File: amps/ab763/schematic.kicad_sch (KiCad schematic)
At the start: 116 parts, among them T1 125P33A, T2 125C3A, T3 125A1A, T4 125A20B

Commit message: Fix: the AB763 phase inverter's two halves sat on the wrong pins, on both the sheet and the board
On the C-FD layout page the 12AT7 inverter's +170 V plate lead, the 82k (hot)
side that the mix node's .001 feeds, lands on pin 1. The +180 V plate (the
100k, cold side) lands on pin 6, and +77 V is on the joined cathodes. The hot
half is therefore unit 2 (pins 1/2/3) and the cold half unit 1 (6/7/8). The
sheet drew V6A/V6B at the default map (A → unit 1), and the board wired the
hot plate, grid and coupler to pins 6/7 and the cold ones to 1/2. The two
surfaces agreed with each other and both disagreed with the page, so the
sheet↔board check could not see it. The blackface board agent found it; it
is confirmed here at native size (layout 6026 × 3650).

- Sheet: V6A unit=2, V6B unit=1, citing the page.
- Board: pins 1↔6, 2↔7, 3↔8 exchanged on the eight inverter runs (both plate
  loads, both couplers C1/C2, both grid leaks, both cathodes to the tail).
  Vias fanned with pipeline/_route.py.

verify_schematic_nets ab763: PASS (claimed). verify_layout_nets ab763: PASS
(the checker solves the section assignment, so no modelled net moves).
Collision lint 0. Both claims keep their fields. What changes is the pin
numbering both drawings print, which is a fact under each claim.

Co-Authored-By: Claude Opus 5 (1M context) <noreply@anthropic.com>
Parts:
- V6A: Basing_unit (none) -> 2
- V6B: Basing_unit (none) -> 1
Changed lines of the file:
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@@
     (in_bom yes) (on_board yes)
     (property "Reference" "V6A" (at 273.7 69.878 0) (effects (font (size 1.27 1.27)) (justify left)))
-    (property "Value" "12AT7" (at 273.7 72.278 0) (effects (font (size 1.27 1.27)) (justify left))))
+    (property "Value" "12AT7" (at 273.7 72.278 0) (effects (font (size 1.27 1.27)) (justify left)))
+    (property "Basing_unit" "2" (at 273.7 74.678 0) (effects (font (size 1.27 1.27)) hide)))
   (symbol (lib_id "cx:TRIODE") (at 267.7 108.278 0) (unit 1)
     (in_bom yes) (on_board yes)
     (property "Reference" "V6B" (at 273.7 101.878 0) (effects (font (size 1.27 1.27)) (justify left)))
-    (property "Value" "12AT7" (at 273.7 104.278 0) (effects (font (size 1.27 1.27)) (justify left))))
+    (property "Value" "12AT7" (at 273.7 104.278 0) (effects (font (size 1.27 1.27)) (justify left)))
+    (property "Basing_unit" "1" (at 273.7 106.678 0) (effects (font (size 1.27 1.27)) hide)))
   (wire (pts (xy 267.7 68.658) (xy 267.7 65.178))
     (stroke (width 0) (type default)))
@@
   (text "3" (at 106.55 192.628 0)
     (effects (font (size 1.1 1.1)) (justify left)))
-  (text "6" (at 268.55 69.928 0)
-    (effects (font (size 1.1 1.1)) (justify left)))
-  (text "7" (at 260.753 74.878 0)
-    (effects (font (size 1.1 1.1)) (justify left)))
-  (text "8" (at 270 82.628 0)
-    (effects (font (size 1.1 1.1)) (justify left)))
-  (text "1" (at 268.55 101.928 0)
-    (effects (font (size 1.1 1.1)) (justify left)))
-  (text "2" (at 260.753 106.878 0)
-    (effects (font (size 1.1 1.1)) (justify left)))
-  (text "3" (at 268.55 114.628 0)
+  (text "1" (at 268.55 69.928 0)
+    (effects (font (size 1.1 1.1)) (justify left)))
+  (text "2" (at 260.753 74.878 0)
+    (effects (font (size 1.1 1.1)) (justify left)))
+  (text "3" (at 270 82.628 0)
+    (effects (font (size 1.1 1.1)) (justify left)))
+  (text "6" (at 268.55 101.928 0)
+    (effects (font (size 1.1 1.1)) (justify left)))
+  (text "7" (at 260.753 106.878 0)
+    (effects (font (size 1.1 1.1)) (justify left)))
+  (text "8" (at 268.55 114.628 0)
     (effects (font (size 1.1 1.1)) (justify left)))
   (text "3" (at 330.55 61.293 0)

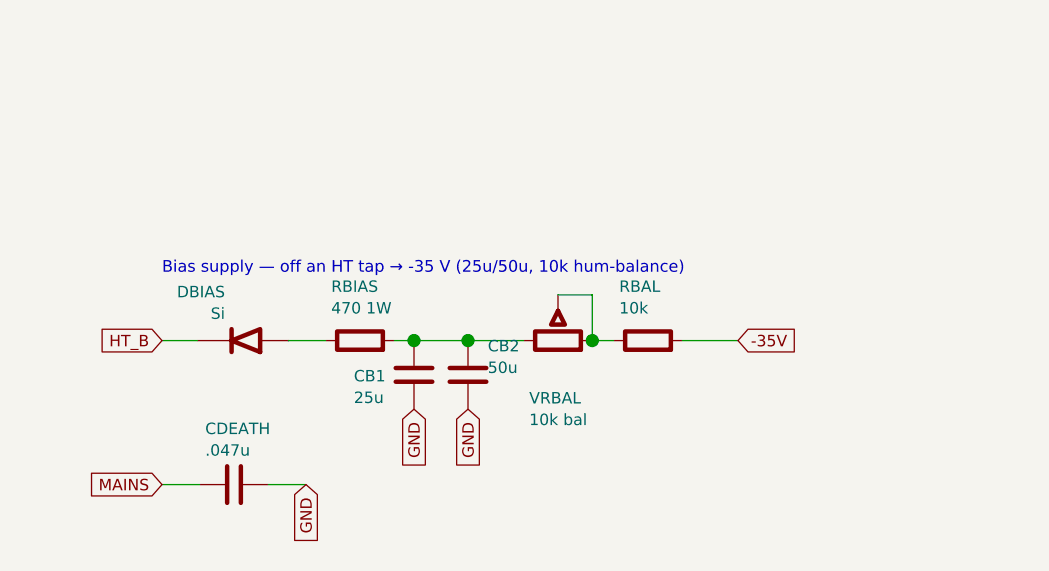
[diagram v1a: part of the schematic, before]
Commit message: Fix: the AB763 sheet drew the bias control as a rheostat in series; the drawing divides the raw supply to ground
The C-FD schematic, read at native size, runs the 10K-L bias control from the
raw negative supply (the node with the rectifier, the 470 and the 25/50 µF
cans) to a 10k (RBAL) that returns to ground. The −35 V line to the 6V6 grid
leaks is the control's WIPER. The sheet drew the control as a rheostat in
series with RBAL and took −35 V off RBAL's far end, so there was no path to
ground at all. The board's own declaration had already read it right: "the
schematic hangs it from the pot's end to ground".

- Sheet: VRBAL across raw → RBAL → ground, with −35 V off the wiper. The raw
  end is labelled BIAS RAW, where the tremolo's 2.2M returns (next commit).
- bom.yaml: VRBAL and RBAL roles say what each joins.
The netlist drives the bias line as an ideal −35 V source, so no DC point
moves. The sheet's bias row is not DC-checked.

Co-Authored-By: Claude Opus 5 (1M context) <noreply@anthropic.com>
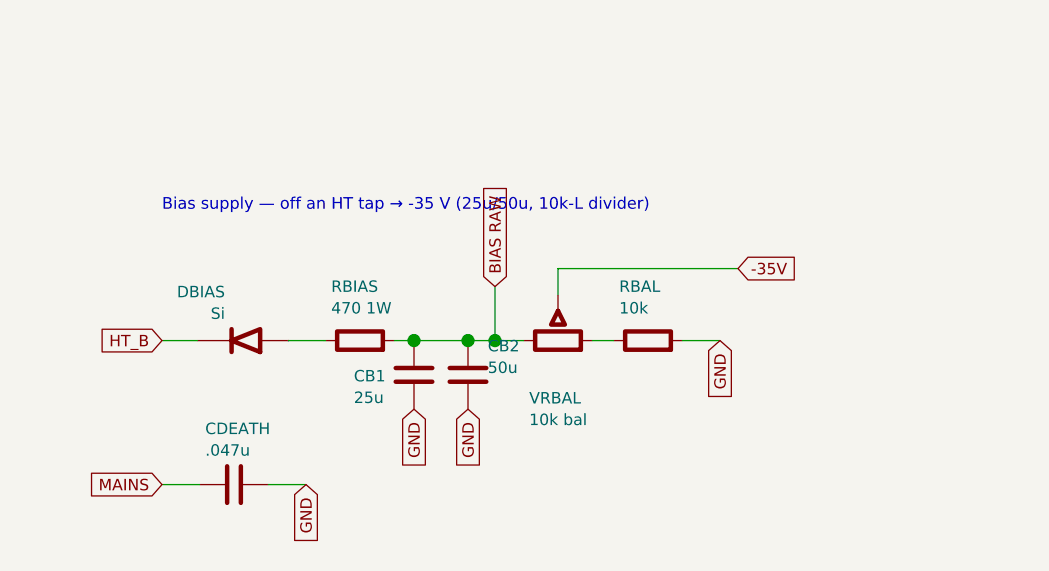
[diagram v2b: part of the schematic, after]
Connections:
- net -35V: now also VRBAL.2 (W); no longer RBAL.2
- net GND: now also RBAL.2
- net BIAS RAW: now reaches CB1.1, CB2.1, RBIAS.2, VRBAL.1
- net at RBAL.1, VRBAL.3: no longer VRBAL.2 (W)
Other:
- note added: "Bias supply — off an HT tap → -35 V (25u/50u, 10k-L divider)"
- note removed: "Bias supply — off an HT tap → -35 V (25u/50u, 10k hum-balance)"
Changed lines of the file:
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@@
   (global_label "GND" (shape input) (at 173.7 241.898 270)
     (effects (font (size 1.27 1.27)) (justify right)))
-  (text "Bias supply — off an HT tap → -35 V (25u/50u, 10k hum-balance)" (at 199.7 212.278 0)
+  (text "Bias supply — off an HT tap → -35 V (25u/50u, 10k-L divider)" (at 199.7 205.278 0)
     (effects (font (size 1.3 1.3)) (justify left)))
   (global_label "HT_B" (shape input) (at 199.7 220.278 180)
@@
   (global_label "GND" (shape input) (at 233.7 227.898 270)
     (effects (font (size 1.27 1.27)) (justify right)))
-  (wire (pts (xy 233.7 220.278) (xy 239.7 220.278))
+  (wire (pts (xy 233.7 220.278) (xy 236.7 220.278))
+    (stroke (width 0) (type default)))
+  (wire (pts (xy 236.7 220.278) (xy 239.89 220.278))
     (stroke (width 0) (type default)))
   (symbol (lib_id "cx:POT") (at 243.7 220.278 90) (unit 1)
@@
     (property "Reference" "VRBAL" (at 240.5 226.678 270) (effects (font (size 1.27 1.27)) (justify left)))
     (property "Value" "10k bal" (at 240.5 229.078 270) (effects (font (size 1.27 1.27)) (justify left))))
-  (wire (pts (xy 239.7 220.278) (xy 239.89 220.278))
+  (wire (pts (xy 243.7 215.198) (xy 243.7 212.278))
     (stroke (width 0) (type default)))
-  (wire (pts (xy 243.7 215.198) (xy 247.51 215.198))
+  (wire (pts (xy 243.7 212.278) (xy 263.7 212.278))
     (stroke (width 0) (type default)))
-  (wire (pts (xy 247.51 215.198) (xy 247.51 220.278))
-    (stroke (width 0) (type default)))
-  (junction (at 247.51 220.278) (diameter 1.467) (color 0 0 0 0))
+  (global_label "-35V" (shape input) (at 263.7 212.278 0)
+    (effects (font (size 1.27 1.27)) (justify left)))
   (symbol (lib_id "cx:R") (at 253.7 220.278 90) (unit 1)
     (in_bom yes) (on_board yes)
@@
   (wire (pts (xy 247.51 220.278) (xy 249.89 220.278))
     (stroke (width 0) (type default)))
-  (wire (pts (xy 257.51 220.278) (xy 263.7 220.278))
+  (wire (pts (xy 257.51 220.278) (xy 261.7 220.278))
     (stroke (width 0) (type default)))
-  (global_label "-35V" (shape input) (at 263.7 220.278 0)
+  (global_label "GND" (shape input) (at 261.7 220.278 270)
+    (effects (font (size 1.27 1.27)) (justify right)))
+  (junction (at 236.7 220.278) (diameter 1.467) (color 0 0 0 0))
+  (wire (pts (xy 236.7 220.278) (xy 236.7 214.278))
+    (stroke (width 0) (type default)))
+  (global_label "BIAS RAW" (shape input) (at 236.7 214.278 90)
     (effects (font (size 1.27 1.27)) (justify left)))
   (global_label "MAINS" (shape input) (at 199.7 236.278 180)

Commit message: Fix: the AB763 tremolo was drawn as a circuit the drawing does not have
The C-FD schematic, read at native size, draws the tremolo as follows:
- V5A is a phase-shift oscillator. Its plate feeds a .02 → .01 → .01 ladder
  back to its own grid. The ladder's middle node goes to ground through the
  3M-RA Speed rheostat and a 100k. The outer node and the grid each reach the
  vibrato-pedal node through a 1M. A 2.2M returns that node to the raw
  negative bias supply, the node ahead of the 10K-L bias control, and the
  footswitch grounds it.
- V5B's grid is DC-coupled to the ladder's outer node. Its plate (+345 V) is
  fed from +415 V (box [B]) through a 10M, and through the neon lamp and a
  100k in series. Both cathodes are bypassed: 2.7k and 100k, each with
  25 µF.
- The photocell sits in the 50K-RA Intensity control's wiper. Intensity's
  top takes the node between the mix driver's .1 and its 220k (the mix
  output, sheet label TREM), and its bottom goes to ground.
The sheet had instead drawn a different oscillator:
- plate loads to B+4;
- the .02 into V5B's grid, with the 10M as V5B's grid leak and the 2.2M as
  V5A's grid leak;
- a plate-to-grid ladder with 1Ms to ground;
- Intensity in the lamp's drive;
- the photocell on the mix-driver grid.
It also lacked both cathode bypass caps and the lamp's 100k. The tremolo is
excluded from the DC netlist (V5 declared in meta.yaml `sections:`), so no
gate compared it with anything. The blackface board agent's independent read
agrees on the 2.2M's return.

- Sheet: the tremolo block redrawn as above. The 2.2M takes the BIAS RAW
  label from the previous commit, and a TREM label marks the mix output.
  MIXG no longer carries the photocell. check_schematics: no isolated pins.
  A per-anchor scan finds no dangling label.
- bom.yaml: CKTO1 and CKTO2 (25 µF · 25 V) and RLAMP (100 kΩ) added. Every
  tremolo part's role now says what it joins. RTO1 is the speed network's
  100k to ground, as the layout also letters it, not a plate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
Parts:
- removed C13: 16u, symbol cx:C
- removed RBIAS: 470 1W, symbol cx:R
- removed RLPA: 82k 5%, symbol cx:R
- removed RNFB: 820, symbol cx:R
- removed RTOG3: 1M, symbol cx:R
- removed T1: 125P33A, symbol cx:PT
- added CB2: 50u, symbol cx:C
- added CTO3: .02u, symbol cx:C
- added RBAL: 10k, symbol cx:R
- added RGPB: 1M, symbol cx:R
- added RLAMP: 100k, symbol cx:R
- added RTOG: 2.2M, symbol cx:R
- added V8: 6V6GT, symbol cx:PENTODE
- added V9B: GZ34, symbol cx:DIODE_TUBE
- added VRINT: 50k int, symbol cx:POT
- C13: renamed from CB2; value 50u -> 16u
- C2: renamed from V8; value 6V6GT -> .1u; symbol cx:PENTODE -> cx:C
- CKTO1: renamed from RTOG; value 2.2M -> 25u; symbol cx:R -> cx:C
- CKTO2: renamed from VRINT; value 50k int -> 25u; symbol cx:POT -> cx:C
- RBIAS: renamed from RBAL; value 10k -> 470 1W
- RLPA: renamed from RTAIL; value 470 -> 82k 5%
- RNFB: renamed from C2; value .1u -> 820; symbol cx:C -> cx:R
- RTAIL: renamed from RGPB; value 1M -> 470
- RTOG3: renamed from CTO3; value .02u -> 1M; symbol cx:C -> cx:R
- T1: renamed from V9B; value GZ34 -> 125P33A; symbol cx:DIODE_TUBE -> cx:PT
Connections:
- net B+1: now also V9B.2 (K); no longer T1.2 (K), T4.2 (PRI_B)
- net B+2: now also RTO10.1, RTO2.1, RLAMP.1
- net B+3: now also RLPA.1
- net B+4: now also C13.1; no longer RTO1.1, RTO2.1
- net BIAS RAW: now also RBIAS.2, CB2.1, RTOG.2; no longer C13.1
- net GND: now also CKTO2.2, RTO1.2, T1.4 (HT_CT), CB2.2, RBAL.2, V8.4 (K), VRINT.1; no longer C2.4 (K), CKTO2.3, OPTO.2 (L2), RBIAS.2, RTO10.2, RTOG2.2, VRSPD.3
- net HT_A: now also T1.3 (HT_A)
- net HT_B: now also T1.5 (HT_B), V9B.1 (A); no longer T1.1 (A)
- net MAINS: now also T1.1 (PRI_1)
- net MAINS N: now also T1.2 (PRI_2)
- net MIXG: no longer OPTO.3 (P1)
- net SPKR: now also RNFB.1
- net at RKTO2.1, V5B.3 (K): now also CKTO2.1
- net at CPIB.1, RNF2.1: now also RNFB.2
- net at RLPB.2, V6B.1 (P): now also C2.1; no longer RNFB.1
- net at C2.2, RGL2.1: now also V8.2 (G1); no longer RNFB.2
- net at VRBN.1, VRBN.2 (W), VRTN.3: no longer CBN.2
- net at RTO2.2, V5A.1 (P): now also CTO3.2; no longer CTO1.2, RTOG3.1
- net at RKTO1.1, V5A.3 (K): now also CKTO1.1
- net at V4A.1 (P), V4B.1 (P): no longer T4.1 (PRI_P)
- net at T3.3 (PRI_B): now also V8.1 (P); no longer C2.1 (P)
- net at RS2.1: now also V8.3 (G2); no longer C2.3 (G2)
- net at CPIB.2, V6B.2 (G): now also RGPB.2; no longer RTAIL.2
- net at V6A.3 (K), V6B.3 (K): now also RTAIL.2; no longer RLPA.2
- net at C1.1, V6A.1 (P): now also RLPA.2
- net at RSLN.1, VRBN.3: no longer CBN2.2
- net at CBV.2, VRBV.1, VRTV.3: no longer VRBV.2 (W)
- net at RGPA.2, RT2.1, RTAIL.1: now also RGPB.1; no longer RLPA.1
- net at OPTO.1 (L1): now also RLAMP.2; no longer CKTO2.2 (W)
- net at CBRV.1, VRVV.1: no longer VRTV.2 (W)
- net TREM: now reaches CCD1.2, RMD1.1
- net TREM: now also VRINT.3
- net at DBIAS.1 (A): now also RBIAS.1
- net at VRBAL.3: now also RBAL.1; no longer RBIAS.1
- new net: OPTO.2 (L2), RTO10.2, V5B.1 (P)
- new net: RTO1.1, VRSPD.2 (W), VRSPD.3
- new net: CTO1.2, RTOG3.2, V5A.2 (G)
- new net: OPTO.3 (P1), VRINT.2 (W)
- new net LFO: CTO1.1, CTO2.1, RTOG2.2
- new net SPEED: CTO2.2, CTO3.1, VRSPD.1
- new net VIB PEDAL: RTOG.1, RTOG2.1, RTOG3.1
- now unconnected: V5B.2 (G)
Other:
- note added: "Tremolo (V5) + optocoupler — a running oscillator, excluded from the DC netlist"
- note removed: "Tremolo oscillator (V5) + optocoupler — dynamic; DC point excluded from netlist (see the circuit story)"
- moved on the sheet: C13, CBD1, CBN, CBN2, CBRV, CBV, CBV2, CCD1, CCN2, CCR1, CCV2, CKN1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

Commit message: Fix: letter the AB763 tremolo bottle's sections as the factory layout pins them
On the C-FD layout page the tremolo 12AX7's +270 V oscillator plate is pin 1,
with the +2.1 V cathode on pin 3. The +345 V lamp-driver plate therefore sits
on pin 6. The sheet had drawn both sections at the default map (A → unit 1).
They are now stated: V5A unit=2, V5B unit=1. The board drawn in the next
commit wires them the same way.

Co-Authored-By: Claude Opus 5 (1M context) <noreply@anthropic.com>
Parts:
- V5A: Basing_unit (none) -> 2
- V5B: Basing_unit (none) -> 1
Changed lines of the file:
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@@
     (in_bom yes) (on_board yes)
     (property "Reference" "V5A" (at 73.6088 195.878 0) (effects (font (size 1.27 1.27)) (justify left)))
-    (property "Value" "12AX7" (at 73.6088 198.278 0) (effects (font (size 1.27 1.27)) (justify left))))
+    (property "Value" "12AX7" (at 73.6088 198.278 0) (effects (font (size 1.27 1.27)) (justify left)))
+    (property "Basing_unit" "2" (at 73.6088 200.678 0) (effects (font (size 1.27 1.27)) hide)))
   (wire (pts (xy 43.6088 202.278) (xy 59.9888 202.278))
     (stroke (width 0) (type default)))
@@
     (in_bom yes) (on_board yes)
     (property "Reference" "V5B" (at 113.609 195.878 0) (effects (font (size 1.27 1.27)) (justify left)))
-    (property "Value" "12AX7" (at 113.609 198.278 0) (effects (font (size 1.27 1.27)) (justify left))))
+    (property "Value" "12AX7" (at 113.609 198.278 0) (effects (font (size 1.27 1.27)) (justify left)))
+    (property "Basing_unit" "1" (at 113.609 200.678 0) (effects (font (size 1.27 1.27)) hide)))
   (wire (pts (xy 93.6088 202.278) (xy 99.9888 202.278))
     (stroke (width 0) (type default)))
@@
   (text "8" (at 224.459 156.628 0)
     (effects (font (size 1.1 1.1)) (justify left)))
-  (text "6" (at 68.4588 195.928 0)
-    (effects (font (size 1.1 1.1)) (justify left)))
-  (text "7" (at 60.6616 200.878 0)
-    (effects (font (size 1.1 1.1)) (justify left)))
-  (text "8" (at 68.4588 208.628 0)
-    (effects (font (size 1.1 1.1)) (justify left)))
-  (text "1" (at 108.459 195.928 0)
-    (effects (font (size 1.1 1.1)) (justify left)))
-  (text "2" (at 100.662 200.878 0)
-    (effects (font (size 1.1 1.1)) (justify left)))
-  (text "3" (at 108.459 208.628 0)
+  (text "1" (at 68.4588 195.928 0)
+    (effects (font (size 1.1 1.1)) (justify left)))
+  (text "2" (at 60.6616 200.878 0)
+    (effects (font (size 1.1 1.1)) (justify left)))
+  (text "3" (at 68.4588 208.628 0)
+    (effects (font (size 1.1 1.1)) (justify left)))
+  (text "6" (at 108.459 195.928 0)
+    (effects (font (size 1.1 1.1)) (justify left)))
+  (text "7" (at 100.662 200.878 0)
+    (effects (font (size 1.1 1.1)) (justify left)))
+  (text "8" (at 108.459 208.628 0)
     (effects (font (size 1.1 1.1)) (justify left)))
   (text "1" (at 266.459 69.928 0)

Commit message: Fix: the AB763 sheet grounded the phase inverter's tail; it now ends at the feedback node
The claim fields are untouched. This follows the model change in the previous
commit, from the same C-FD reading (schematic page, crop sch-pi-tail, 740 x 1080
at 2560,680 of the 6070 x 4274 native image): the 22K's far end is a junction
on the vertical lead that brings the 820 down from the speaker, with the
.1-200 from the cold grid and the 47 to ground hanging below it.

- Sheet (pipeline/draw_ab763.py, regenerated): RT2's foot drops onto CPIB's
  far-side wire, the feedback node, in place of its ground symbol, with a
  junction where it lands. RT2.2 now shares a net with RNF2.1, RNFB.2 and
  CPIB.1. verify_schematic_nets ab763: PASS (claimed), with RNFB, now in the
  model, checked end to end. check_schematics: 0 failures, connectivity clean
  (no isolated pin, no dangling label, no shorted part). The preview
  (pipeline/_sch_preview.py) of the inverter was looked at before and after:
  the only change is the foot, and the RT2 / 22k lettering sits where it did.
- bom.yaml: the RT2, RNFB and RNF2 roles say what they join.
- notes.md: the inverter paragraph names the tail's foot and the 47. The chart
  paragraph said the inverter plates and tail "fall within a tenth" of the
  chart; the 82k plate is 10.5 % high, so it now says "about a tenth" and
  names that plate.

reference/sheet-board.yaml is re-exported: RT2 is MISPLACED on ab763 (the
board still grounds the tail) until the board follows in the next commit, so
verify_layout_nets ab763 still FAILS at this commit.

Co-Authored-By: Claude Opus 5.5 <noreply@anthropic.com>
Claude-Session: https://claude.ai/code/session_01KBMfdh37HmCL2iWcBiL5J1
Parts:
- removed C11, C12: 16u, symbol cx:C
- removed V7, V8: 6V6GT, symbol cx:PENTODE
- added RD1, RD2: 10k, symbol cx:R
- added RGL1, RGL2: 220k, symbol cx:R
- C11: renamed from RD1; value 10k -> 16u; symbol cx:R -> cx:C
- C12: renamed from RD2; value 10k -> 16u; symbol cx:R -> cx:C
- V7: renamed from RGL1; value 220k -> 6V6GT; symbol cx:R -> cx:PENTODE
- V8: renamed from RGL2; value 220k -> 6V6GT; symbol cx:R -> cx:PENTODE
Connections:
- net -35V: now also RGL1.2, RGL2.2; no longer V7.2, V8.2
- net B+2: now also RD1.1
- net B+3: now also RD1.2, RD2.1; no longer C11.2
- net B+4: now also RD2.2; no longer C12.2
- net GND: now also C11.2, C12.2, V7.4 (K), V8.4 (K); no longer RT2.2
- net at T3.1 (PRI_A): now also V7.1 (P)
- net at C1.2: now also V7.2 (G1), RGL1.1; no longer V7.1
- net at RS1.1: now also V7.3 (G2)
- net at RS2.1: now also V8.3 (G2)
- net at CPIB.1, RNF2.1, RNFB.2: now also RT2.2
- net at C2.2: now also V8.2 (G1), RGL2.1; no longer V8.1
- net at T3.3 (PRI_B): now also V8.1 (P)
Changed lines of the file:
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@@
     (property "Reference" "RT2" (at 241.809 92.888 0) (effects (font (size 1.27 1.27)) (justify left)))
     (property "Value" "22k" (at 241.809 95.288 0) (effects (font (size 1.27 1.27)) (justify left))))
-  (global_label "GND" (shape input) (at 239.609 99.898 270)
-    (effects (font (size 1.27 1.27)) (justify right)))
+  (wire (pts (xy 239.609 99.898) (xy 239.609 108.278))
+    (stroke (width 0) (type default)))
+  (junction (at 239.609 108.278) (diameter 1.46) (color 0 0 0 0))
   (symbol (lib_id "cx:R") (at 243.609 84.278 0) (unit 1)
     (in_bom yes) (on_board yes)
@@
     (stroke (width 0) (type default)))
   (junction (at 257.989 108.278) (diameter 1.46) (color 0 0 0 0))
-  (wire (pts (xy 241.799 108.278) (xy 231.609 108.278))
+  (wire (pts (xy 241.799 108.278) (xy 239.609 108.278))
+    (stroke (width 0) (type default)))
+  (wire (pts (xy 239.609 108.278) (xy 231.609 108.278))
     (stroke (width 0) (type default)))
   (global_label "SPKR" (shape input) (at 205.609 120.278 180)
